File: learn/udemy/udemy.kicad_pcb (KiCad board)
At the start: 2 copper layers, 13 parts, among them J1 Screw_Terminal_01x02, J2 Screw_Terminal_01x02, J3 Screw_Terminal_01x02, U1 L7809, U2 L7805

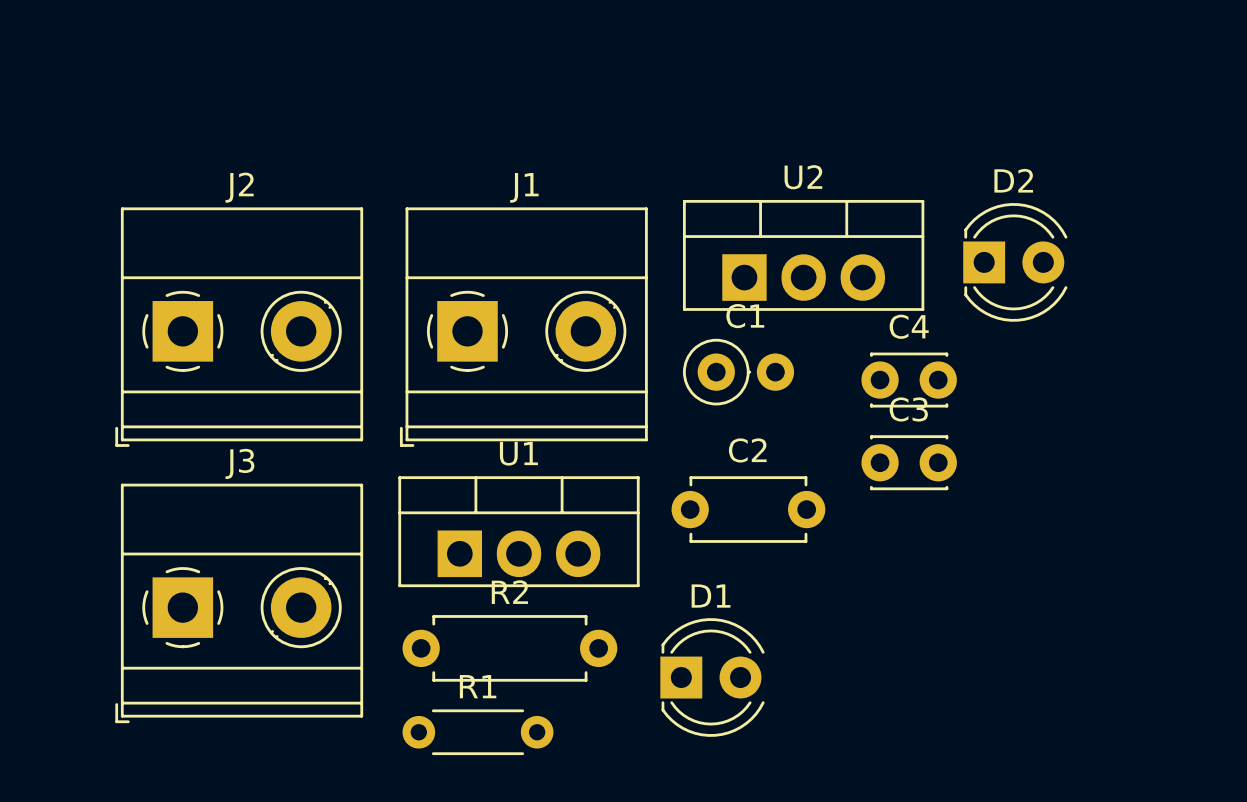
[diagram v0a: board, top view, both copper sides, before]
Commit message: 08/01/23 sistemato i componenti nella pcb
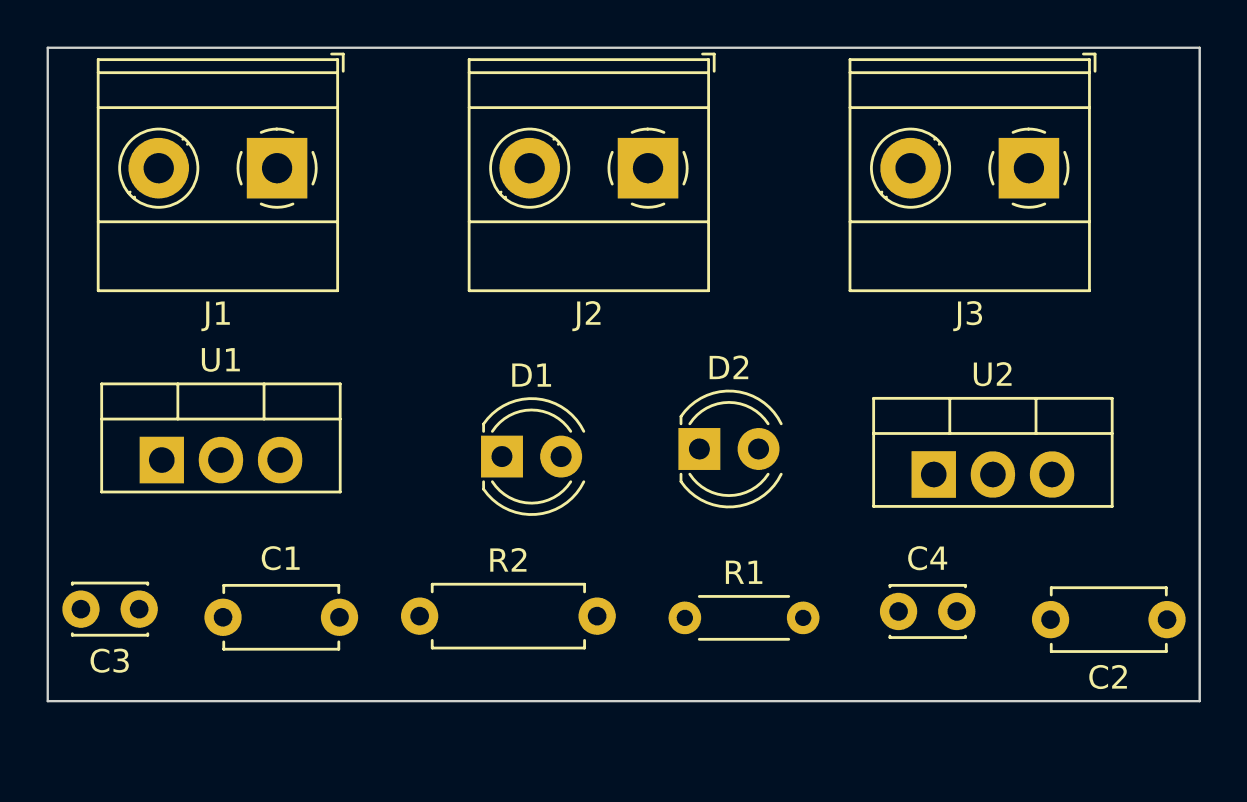
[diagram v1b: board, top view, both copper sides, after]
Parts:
- C1: footprint Resistor_THT:R_Axial_DIN0207_L6.3mm_D2.5mm_P2.54mm_Vertical -> Capacitor_THT:C_Disc_D4.7mm_W2.5mm_P5.00mm
- moved J3 40.9 mm to (158.3, 59.9), turned to 180 degrees
- moved C3 32.4 mm to (120.1, 78.9), turned to 180 degrees
- moved C1 23.6 mm to (123.7, 79.2)
- moved J2 21.2 mm to (141.9, 59.9), turned to 180 degrees
- moved C2 21.0 mm to (164.2, 79.3), turned to 180 degrees
- moved D2 14.6 mm to (144.2, 72.0)
- moved U1 13.4 mm to (121.1, 72.5)
- moved R1 12.4 mm to (143.5, 79.2)
- moved D1 12.2 mm to (135.7, 72.3)
- moved U2 11.7 mm to (154.2, 73.1)
- moved J1 10.8 mm to (126.0, 59.9), turned to 180 degrees
- moved C4 9.97 mm to (152.7, 79.0)
- moved R2 1.39 mm to (132.1, 79.2)
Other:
- board outline added: 49.5 x 28.1 mm
